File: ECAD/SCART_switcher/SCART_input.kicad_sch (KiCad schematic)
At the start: 35 parts, among them J1 SCART-F, Q1 BC847, Q2 BC847, Q3 BC847, U1 THS7374, U3 74AHC1G00, U4 74AHC1G02, U8 74AHC1G08

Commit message: Progressed ECAD.
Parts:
- C1, C2, C3, C4: footprint (none) -> Capacitor_SMD:C_0805_2012Metric_Pad1.18x1.45mm_HandSolder
- R17: value 1kR -> 800R
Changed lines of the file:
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@@
       (effects (font (size 1.27 1.27)))
     )
-    (property "Footprint" "" (at 74.93 155.2448 0)
+    (property "Footprint" "Capacitor_SMD:C_0805_2012Metric_Pad1.18x1.45mm_HandSolder" (at 74.93 155.2448 0)
       (effects (font (size 1.27 1.27)) hide)
     )
@@
       (effects (font (size 1.27 1.27)) (justify left))
     )
-    (property "Value" "1kR" (at 250.952 62.23 0)
+    (property "Value" "800R" (at 250.952 62.23 0)
       (effects (font (size 1.27 1.27)) (justify left))
     )
@@
       (effects (font (size 1.27 1.27)))
     )
-    (property "Footprint" "" (at 74.93 164.1348 0)
+    (property "Footprint" "Capacitor_SMD:C_0805_2012Metric_Pad1.18x1.45mm_HandSolder" (at 74.93 164.1348 0)
       (effects (font (size 1.27 1.27)) hide)
     )
@@
       (effects (font (size 1.27 1.27)))
     )
-    (property "Footprint" "" (at 74.93 146.3548 0)
+    (property "Footprint" "Capacitor_SMD:C_0805_2012Metric_Pad1.18x1.45mm_HandSolder" (at 74.93 146.3548 0)
       (effects (font (size 1.27 1.27)) hide)
     )
@@
       (effects (font (size 1.27 1.27)))
     )
-    (property "Footprint" "" (at 74.93 173.0248 0)
-      (effects (font (size 1.27 1.27)) hide)
-    )
+    (property "Footprint" "Capacitor_SMD:C_0805_2012Metric_Pad1.18x1.45mm_HandSolder" (at 74.93 173.0248 0)
+      (effects (font (size 1.27 1.27)) hide)
+    )

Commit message: Progressed ECAD.
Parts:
- Q1, Q2, Q3: MFN (none) -> BC847B,215
- U1: MFN (none) -> THS7374IPWR
- U3: footprint (none) -> Package_TO_SOT_SMD:SOT-23-5; MFN (none) -> 74AHC1G00W5-7
- U4: footprint (none) -> Package_TO_SOT_SMD:SOT-23-5; MFN (none) -> 74AHC1G02W5-7
- U8: footprint (none) -> Package_TO_SOT_SMD:SOT-23-5; MFN (none) -> 74AHC1G08W5-7
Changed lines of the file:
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@@
       (effects (font (size 1.27 1.27)) hide)
     )
+    (property "MFN" "" (at 59.69 180.34 0)
+      (effects (font (size 1.27 1.27)) hide)
+    )
     (pin "1")
     (pin "2")
@@
       (effects (font (size 1.27 1.27)) hide)
     )
+    (property "MFN" "" (at 233.68 60.96 0)
+      (effects (font (size 1.27 1.27)) hide)
+    )
     (pin "1")
     (pin "2")
@@
       (effects (font (size 1.27 1.27)) hide)
     )
+    (property "MFN" "" (at 36.83 180.34 0)
+      (effects (font (size 1.27 1.27)) hide)
+    )
     (pin "1")
     (pin "2")
@@
       (effects (font (size 1.27 1.27)) hide)
     )
+    (property "MFN" "" (at 129.54 165.1 0)
+      (effects (font (size 1.27 1.27)) hide)
+    )
     (pin "1")
     (pin "2")
@@
       (effects (font (size 1.27 1.27)) hide)
     )
+    (property "MFN" "" (at 241.3 55.88 0)
+      (effects (font (size 1.27 1.27)) hide)
+    )
     (pin "1")
     (pin "2")
@@
       (effects (font (size 1.27 1.27)) hide)
     )
+    (property "MFN" "" (at 71.12 156.21 0)
+      (effects (font (size 1.27 1.27)) hide)
+    )
     (pin "1")
     (pin "2")
@@
       (effects (font (size 1.27 1.27)) hide)
     )
+    (property "MFN" "" (at 264.16 130.81 0)
+      (effects (font (size 1.27 1.27)) hide)
+    )
     (pin "1")
     (pin "2")
@@
       (effects (font (size 1.27 1.27)) hide)
     )
+    (property "MFN" "" (at 264.16 95.25 0)
+      (effects (font (size 1.27 1.27)) hide)
+    )
     (pin "1")
     (pin "2")
@@
       (effects (font (size 1.27 1.27)) hide)
     )
+    (property "MFN" "" (at 207.01 54.61 0)
+      (effects (font (size 1.27 1.27)) hide)
+    )
     (pin "1")
     (pin "2")
@@
       (effects (font (size 1.27 1.27)) hide)
     )
+    (property "MFN" "" (at 44.45 180.34 0)
+      (effects (font (size 1.27 1.27)) hide)
+    )
     (pin "1")
     (pin "2")
@@
       (effects (font (size 1.27 1.27)) hide)
     )
+    (property "MFN" "" (at 201.93 25.4 0)
+      (effects (font (size 1.27 1.27)) hide)
+    )
     (pin "1")
     (pin "2")
@@
       (effects (font (size 1.27 1.27)))
     )
-    (property "Footprint" "" (at 224.79 95.25 0)
+    (property "Footprint" "Package_TO_SOT_SMD:SOT-23-5" (at 224.79 95.25 0)
       (effects (font (size 1.27 1.27)) hide)
     )
-    (property "Datasheet" "http://www.ti.com/lit/sg/scyt129e/scyt129e.pdf" (at 224.79 95.25 0)
+    (property "Datasheet" "https://datasheet.lcsc.com/lcsc/2201131130_Diodes-Incorporated-74AHC1G00W5-7_C842261.pdf" (at 224.79 95.25 0)
+      (effects (font (size 1.27 1.27)) hide)
+    )
+    (property "MFN" "74AHC1G00W5-7" (at 224.79 95.25 0)
       (effects (font (size 1.27 1.27)) hide)
     )
@@
       (effects (font (size 1.27 1.27)))
     )
-    (property "Footprint" "" (at 105.41 114.3 0)
+    (property "Footprint" "Package_TO_SOT_SMD:SOT-23-5" (at 105.41 114.3 0)
+      (effects (font (size 1.27 1.27)) hide)
+    )
+    (property "Datasheet" "https://datasheet.lcsc.com/lcsc/1912111437_Diodes-Incorporated-74AHC1G08W5-7_C460487.pdf" (at 105.41 114.3 0)
       (effects (font (size 1.27 1.27)) hide)
     )
-    (property "Datasheet" "http://www.ti.com/lit/sg/scyt129e/scyt129e.pdf" (at 105.41 114.3 0)
+    (property "MFN" "74AHC1G08W5-7" (at 105.41 114.3 0)
       (effects (font (size 1.27 1.27)) hide)
     )
@@
       (effects (font (size 1.27 1.27)) hide)
     )
+    (property "MFN" "" (at 129.54 147.32 0)
+      (effects (font (size 1.27 1.27)) hide)
+    )
     (pin "1")
     (pin "2")
@@
       (effects (font (size 1.27 1.27)) hide)
     )
+    (property "MFN" "" (at 52.07 180.34 0)
+      (effects (font (size 1.27 1.27)) hide)
+    )
     (pin "1")
     (pin "2")
@@
       (effects (font (size 1.27 1.27)) hide)
     )
+    (property "MFN" "" (at 129.54 173.99 0)
+      (effects (font (size 1.27 1.27)) hide)
+    )
     (pin "1")
     (pin "2")
@@
       (effects (font (size 1.27 1.27)) hide)
     )
+    (property "MFN" "" (at 57.15 58.42 0)
+      (effects (font (size 1.27 1.27)) hide)
+    )
     (pin "1")
     (pin "10")
@@
       (effects (font (size 1.27 1.27)) hide)
     )
+    (property "MFN" "" (at 91.44 151.13 0)
+      (effects (font (size 1.27 1.27)) hide)
+    )
     (pin "1")
     (pin "2")
@@
       (effects (font (size 1.27 1.27)) hide)
     )
+    (property "MFN" "" (at 248.92 60.96 0)
+      (effects (font (size 1.27 1.27)) hide)
+    )
     (pin "1")
     (pin "2")
@@
       (effects (font (size 1.27 1.27)) hide)
     )
+    (property "MFN" "" (at 71.12 165.1 0)
+      (effects (font (size 1.27 1.27)) hide)
+    )
     (pin "1")
     (pin "2")
@@
       (effects (font (size 1.27 1.27)) hide)
     )
+    (property "MFN" "" (at 71.12 147.32 0)
+      (effects (font (size 1.27 1.27)) hide)
+    )
     (pin "1")
     (pin "2")
@@
       (effects (font (size 1.27 1.27)))
     )
-    (property "Footprint" "" (at 224.79 130.81 0)
+    (property "Footprint" "Package_TO_SOT_SMD:SOT-23-5" (at 224.79 130.81 0)
+      (effects (font (size 1.27 1.27)) hide)
+    )
+    (property "Datasheet" "https://datasheet.lcsc.com/lcsc/2201131130_Diodes-Incorporated-74AHC1G02W5-7_C842262.pdf" (at 224.79 130.81 0)
       (effects (font (size 1.27 1.27)) hide)
     )
-    (property "Datasheet" "http://www.ti.com/lit/sg/scyt129e/scyt129e.pdf" (at 224.79 130.81 0)
+    (property "MFN" "74AHC1G02W5-7" (at 224.79 130.81 0)
       (effects (font (size 1.27 1.27)) hide)
     )
@@
       (effects (font (size 1.27 1.27)) hide)
     )
+    (property "MFN" "" (at 129.54 156.21 0)
+      (effects (font (size 1.27 1.27)) hide)
+    )
     (pin "1")
     (pin "2")
@@
       (effects (font (size 1.27 1.27)) hide)
     )
+    (property "MFN" "" (at 48.26 118.11 0)
+      (effects (font (size 1.27 1.27)) hide)
+    )
     (pin "1")
     (pin "2")
@@
       (effects (font (size 1.27 1.27)) hide)
     )
+    (property "MFN" "" (at 248.92 45.72 0)
+      (effects (font (size 1.27 1.27)) hide)
+    )
     (pin "1")
     (pin "2")
@@
       (effects (font (size 1.27 1.27)) hide)
     )
+    (property "MFN" "" (at 207.01 46.99 0)
+      (effects (font (size 1.27 1.27)) hide)
+    )
     (pin "1")
     (pin "2")
@@
       (effects (font (size 1.27 1.27)) hide)
     )
+    (property "MFN" "" (at 60.96 113.03 0)
+      (effects (font (size 1.27 1.27)) hide)
+    )
     (pin "1")
     (pin "2")
@@
       (effects (font (size 1.27 1.27)) hide)
     )
+    (property "MFN" "" (at 220.98 33.02 0)
+      (effects (font (size 1.27 1.27)) hide)
+    )
     (pin "1")
     (pin "2")
@@
       (effects (font (size 1.27 1.27) italic) (justify left) hide)
     )
-    (property "Datasheet" "http://www.infineon.com/dgdl/Infineon-BC847SERIES_BC848SERIES_BC849SERIES_BC850SERIES-DS-v01_01-en.pdf?fileId=db3a304314dca389011541d4630a1657" (at 218.44 50.8 0)
+    (property "Datasheet" "https://datasheet.lcsc.com/lcsc/2304140030_Nexperia-BC847B-215_C57668.pdf" (at 218.44 50.8 0)
       (effects (font (size 1.27 1.27)) (justify left) hide)
     )
+    (property "MFN" "BC847B,215" (at 218.44 50.8 0)
+      (effects (font (size 1.27 1.27)) hide)
+    )
     (pin "1")
     (pin "2")
@@
       (effects (font (size 1.27 1.27)) hide)
     )
+    (property "MFN" "" (at 48.26 125.73 0)
+      (effects (font (size 1.27 1.27)) hide)
+    )
     (pin "1")
     (pin "2")
@@
       (effects (font (size 1.27 1.27) italic) (justify left) hide)
     )
-    (property "Datasheet" "http://www.infineon.com/dgdl/Infineon-BC847SERIES_BC848SERIES_BC849SERIES_BC850SERIES-DS-v01_01-en.pdf?fileId=db3a304314dca389011541d4630a1657" (at 58.42 121.92 0)
+    (property "Datasheet" "https://datasheet.lcsc.com/lcsc/2304140030_Nexperia-BC847B-215_C57668.pdf" (at 58.42 121.92 0)
       (effects (font (size 1.27 1.27)) (justify left) hide)
     )
+    (property "MFN" "BC847B,215" (at 58.42 121.92 0)
+      (effects (font (size 1.27 1.27)) hide)
+    )
     (pin "1")
     (pin "2")
@@
       (effects (font (size 1.27 1.27)) hide)
     )
+    (property "MFN" "" (at 71.12 173.99 0)
+      (effects (font (size 1.27 1.27)) hide)
+    )
     (pin "1")
     (pin "2")
@@
       (effects (font (size 1.27 1.27)) hide)
     )
+    (property "MFN" "" (at 260.35 31.75 0)
+      (effects (font (size 1.27 1.27)) hide)
+    )
     (pin "1")
     (pin "2")
@@
       (effects (font (size 1.27 1.27) italic) (justify left) hide)
     )
-    (property "Datasheet" "http://www.infineon.com/dgdl/Infineon-BC847SERIES_BC848SERIES_BC849SERIES_BC850SERIES-DS-v01_01-en.pdf?fileId=db3a304314dca389011541d4630a1657" (at 257.81 50.8 0)
+    (property "Datasheet" "https://datasheet.lcsc.com/lcsc/2304140030_Nexperia-BC847B-215_C57668.pdf" (at 257.81 50.8 0)
       (effects (font (size 1.27 1.27)) (justify left) hide)
     )
+    (property "MFN" "BC847B,215" (at 257.81 50.8 0)
+      (effects (font (size 1.27 1.27)) hide)
+    )
     (pin "1")
     (pin "2")
@@
       (effects (font (size 1.27 1.27)) hide)
     )
-    (property "Datasheet" "https://www.ti.com/lit/ds/symlink/ths7374.pdf" (at 100.33 173.99 0)
+    (property "Datasheet" "https://datasheet.lcsc.com/lcsc/2106080232_Texas-Instruments-THS7374IPWR_C2652746.pdf" (at 100.33 173.99 0)
+      (effects (font (size 1.27 1.27)) hide)
+    )
+    (property "MFN" "THS7374IPWR" (at 100.33 173.99 0)
       (effects (font (size 1.27 1.27)) hide)
     )

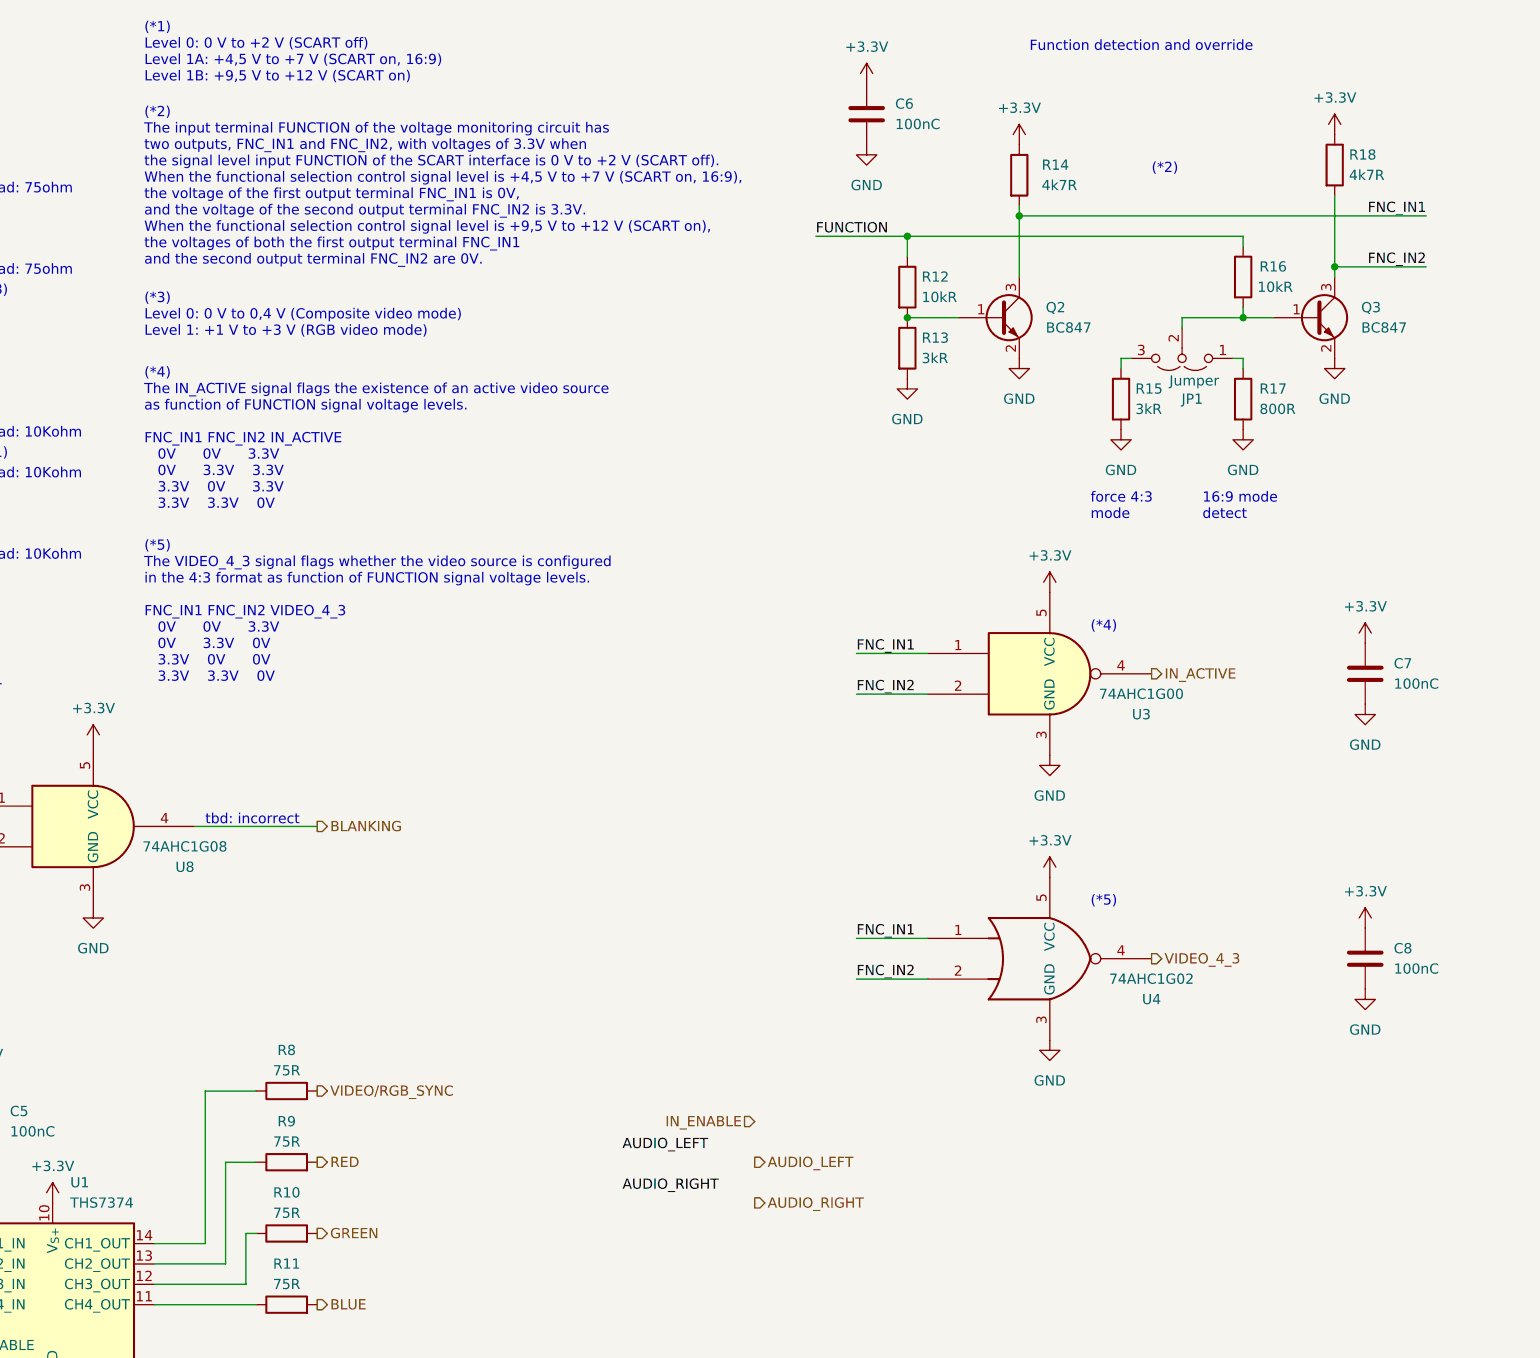
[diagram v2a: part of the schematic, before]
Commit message: Circuit simplification
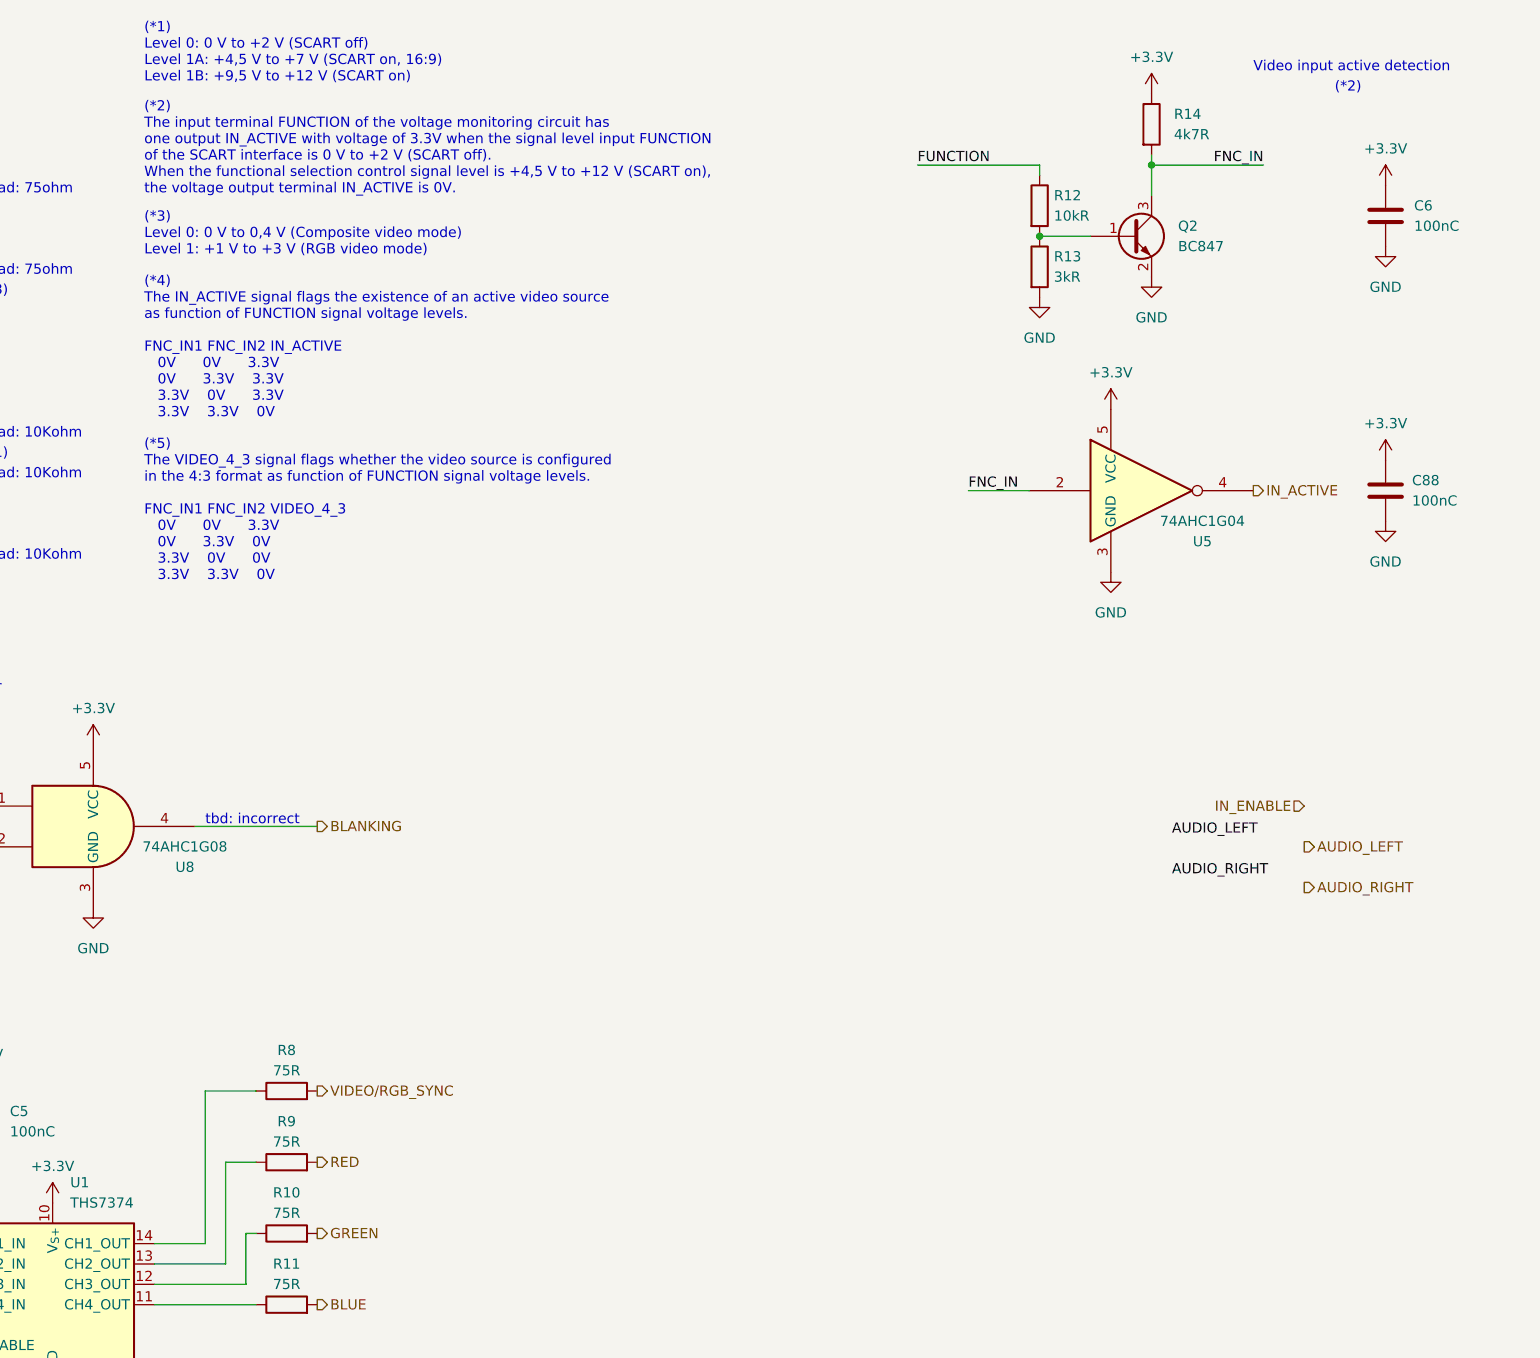
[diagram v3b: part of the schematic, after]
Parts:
- removed C7, C8: 100nC, Capacitor_SMD:C_0805_2012Metric_Pad1.18x1.45mm_HandSolder, symbol Device:C
- removed JP1: Jumper, Connector_PinHeader_2.54mm:PinHeader_1x03_P2.54mm_Vertical, symbol Jumper:Jumper_3_Open
- removed Q3: BC847, Package_TO_SOT_SMD:SOT-23, symbol Transistor_BJT:BC847
- removed R15: 3kR, Resistor_SMD:R_0805_2012Metric_Pad1.20x1.40mm_HandSolder, symbol Device:R
- removed R16: 10kR, Resistor_SMD:R_0805_2012Metric_Pad1.20x1.40mm_HandSolder, symbol Device:R
- removed R17: 800R, Resistor_SMD:R_0805_2012Metric_Pad1.20x1.40mm_HandSolder, symbol Device:R
- removed R18: 4k7R, Resistor_SMD:R_0805_2012Metric_Pad1.20x1.40mm_HandSolder, symbol Device:R
- removed U3: 74AHC1G00, Package_TO_SOT_SMD:SOT-23-5, symbol 74xGxx:74AHC1G00
- removed U4: 74AHC1G02, Package_TO_SOT_SMD:SOT-23-5, symbol 74xGxx:74AHC1G02
- added C88: 100nC, Capacitor_SMD:C_0805_2012Metric_Pad1.18x1.45mm_HandSolder, symbol Device:C
- added U5: 74AHC1G04, Package_TO_SOT_SMD:SOT-23-5, symbol 74xGxx:74AHC1G04
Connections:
- net +3.3V: now also C88.1, U5.5 (VCC)
- net GND: now also C88.2, U5.3 (GND)
- net IN_ACTIVE: now also U5.4
- net FNC_IN1 renamed FNC_IN
- net FNC_IN: now also U5.2
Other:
- note added: "(*2) The input terminal FUNCTION of the voltage monitoring circuit has one output IN_ACTIVE with voltage of 3.3V when the signal level input FUNCTION of the SCART interface is 0 V to +2 V (SCART off). When the functional selection control signal level is +4,5 V to +12 V (SCART on), the voltage output terminal IN_ACTIVE is 0V."
- note added: "Video input active detection"
- note removed: "(*2) The input terminal FUNCTION of the voltage monitoring circuit has two outputs, FNC_IN1 and FNC_IN2, with voltages of 3.3V when the signal level input FUNCTION of the SCART interface is 0 V to +2 V (SCART off). When the functional selection control signal level is +4,5 V to +7 V (SCART on, 16:9), the voltage of the first output terminal FNC_IN1 is 0V, and the voltage of the second output term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"
- note removed: "(*4)"
- note removed: "(*5)"
- note removed: "16:9 mode detect"
- note removed: "Function detection and override"
- note removed: "force 4:3 mode"
- moved on the sheet: C6, Q2, R12, R13, R14

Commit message: Progressed ECAD
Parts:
- removed U8: 74AHC1G08, Package_TO_SOT_SMD:SOT-23-5, symbol 74xGxx:74AHC1G08
- added U10, U2: 74AHC1G126, symbol 74xGxx:74AHC1G126
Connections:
- net +3.3V: now also U10.5 (VCC), U2.5 (VCC)
- net BLANKING: now also U10.4
- net GND: now also U10.3 (GND), U2.3 (GND)
- net IN_ENABLE: now also U10.1, U2.1
- net at Q1.3 (C), R7.2: now also U10.2
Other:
- note removed: "tbd: incorrect"

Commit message: Progressed ECAD.
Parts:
- added C90: 100nC, Capacitor_SMD:C_0805_2012Metric_Pad1.18x1.45mm_HandSolder, symbol Device:C
- added U4: 74LVC2G66, Package_SO:TSSOP-8_3x3mm_P0.65mm, symbol 74xGxx:74AUC2G66
- added U82: TLV9002S, symbol Amplifier_Operational:LTC6269xDD
- C1, C2, C3, C4: value 0.1uC -> 100nC
- renumbered U10 to U2, U2 to U3
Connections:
- net AUDIO_LEFT: now also U4.1, U4.2
- net AUDIO_RIGHT: now also U4.5, U4.6
- net GND: now also C90.2, U4.4 (GND)
- net IN_ENABLE: now also U4.3, U4.7
- new net: U82.11 (V-), U82.4 (V-)
- new net +5V: C90.1, U4.8 (VCC)
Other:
- note added: "Audio switching circuit"
- moved on the sheet: U3
